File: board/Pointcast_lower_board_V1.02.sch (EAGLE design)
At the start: 28 parts, among them U6 Ethernet, X2 3G module, X4 3GS shield

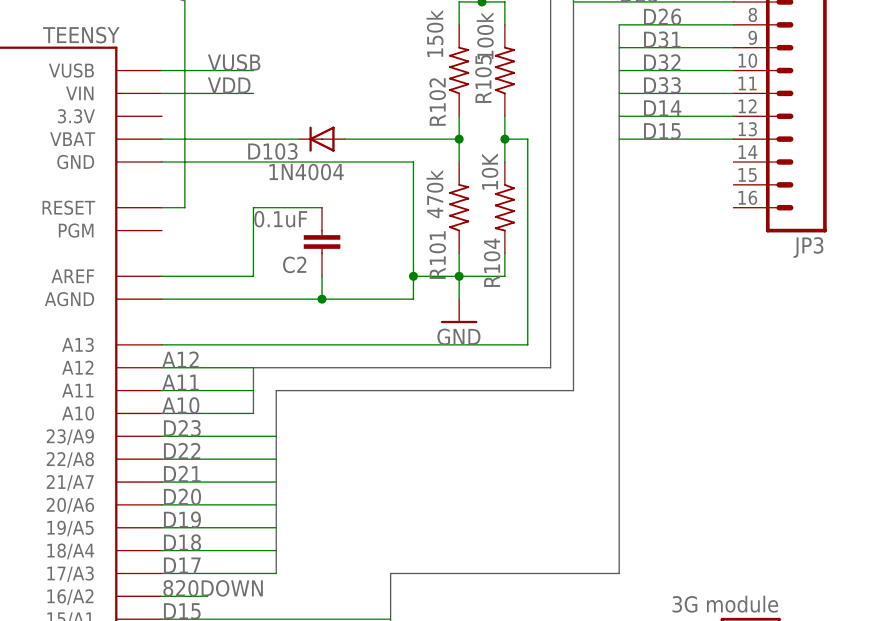
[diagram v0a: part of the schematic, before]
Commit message: V3.7.8 added temperature on main screen, dev and api switch on display, logging header with logs, retarts and fails
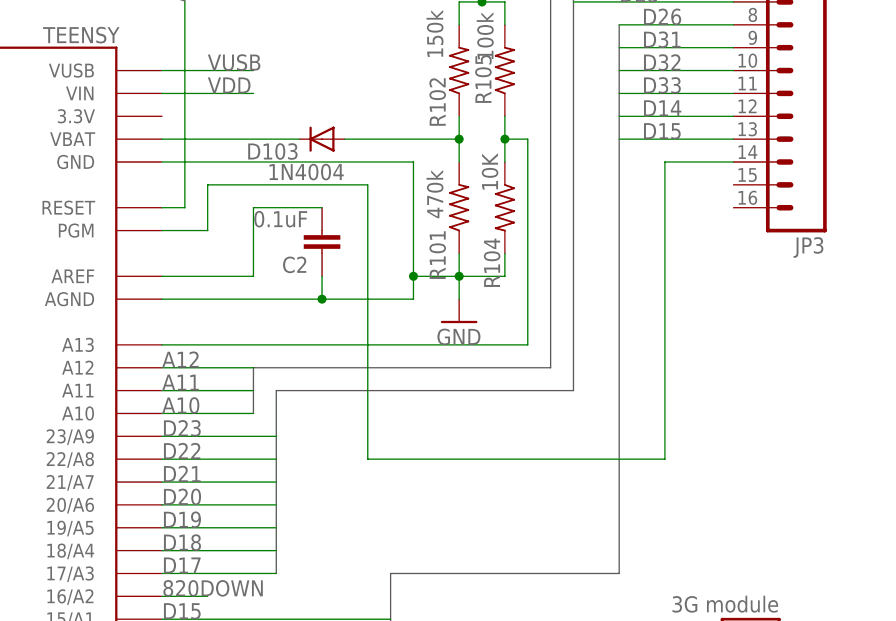
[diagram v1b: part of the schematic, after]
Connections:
- new net N$22: JP3.14, TEENSY.PGM
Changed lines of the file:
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@@
 <?xml version="1.0" encoding="utf-8"?>
 <!DOCTYPE eagle SYSTEM "eagle.dtd">
-<eagle version="7.2.0">
+<eagle version="7.5.0">
 <drawing>
 <settings>
@@
 </segment>
 </net>
+<net name="N$22" class="0">
+<segment>
+<pinref part="JP3" gate="G$1" pin="14"/>
+<wire x1="160.02" y1="198.12" x2="152.4" y2="198.12" width="0.1524" layer="91"/>
+<wire x1="152.4" y1="198.12" x2="152.4" y2="165.1" width="0.1524" layer="91"/>
+<wire x1="152.4" y1="165.1" x2="119.38" y2="165.1" width="0.1524" layer="91"/>
+<wire x1="119.38" y1="165.1" x2="119.38" y2="195.58" width="0.1524" layer="91"/>
+<wire x1="119.38" y1="195.58" x2="101.6" y2="195.58" width="0.1524" layer="91"/>
+<wire x1="101.6" y1="195.58" x2="101.6" y2="190.5" width="0.1524" layer="91"/>
+<pinref part="TEENSY" gate="G$1" pin="PGM"/>
+<wire x1="101.6" y1="190.5" x2="96.52" y2="190.5" width="0.1524" layer="91"/>
+</segment>
+</net>
